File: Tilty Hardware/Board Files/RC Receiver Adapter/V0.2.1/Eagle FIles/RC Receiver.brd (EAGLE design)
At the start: 38.1 x 50.8 mm, 33 parts, among them U1 ATMEGA328P, U2 LM2931, U3 AP7313SOT23R, U4 PCA9306, Y1 16MHz

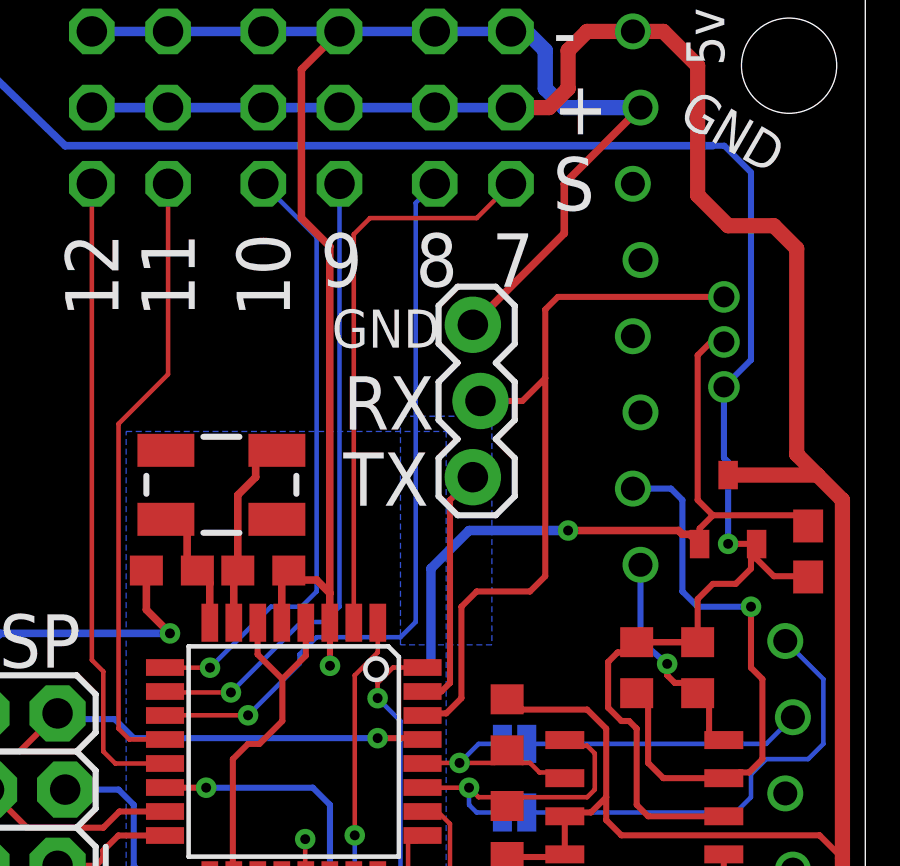
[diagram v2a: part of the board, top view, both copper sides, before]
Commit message: Moved serial breakout slightly
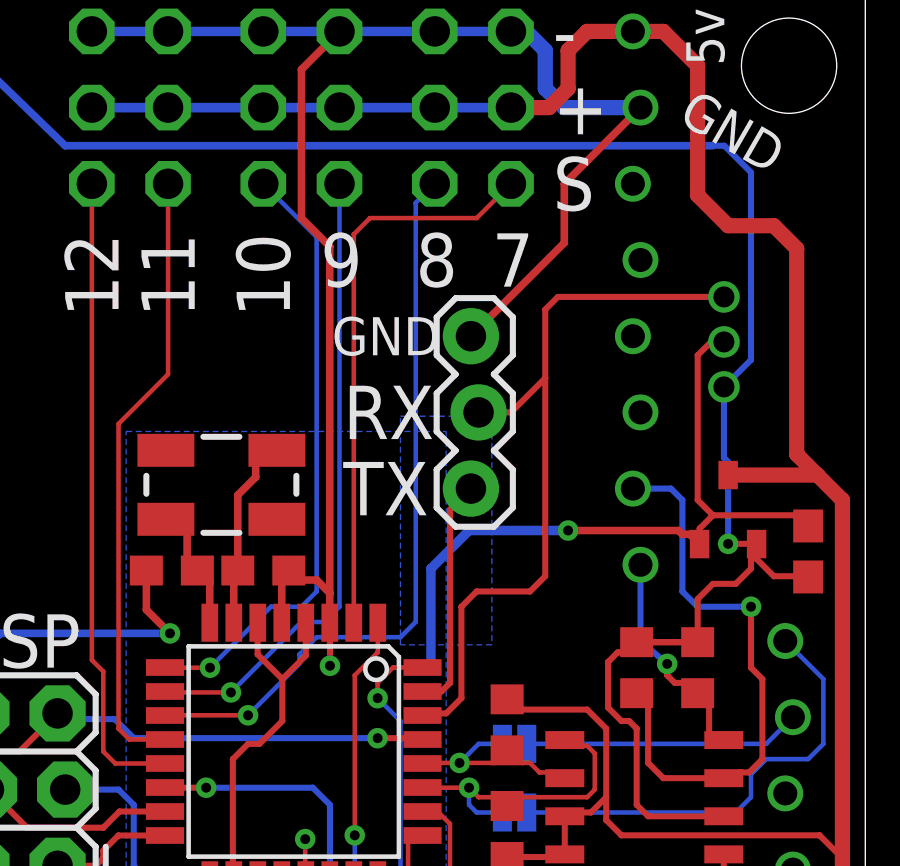
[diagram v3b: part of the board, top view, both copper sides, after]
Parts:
- moved JP9 0.39 mm to (25.1, 34.2)
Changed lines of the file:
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@@
 <text x="5.334" y="46.482" size="1.27" layer="25" ratio="15" rot="R75">3v3</text>
 <text x="35.306" y="9.906" size="1.27" layer="25" ratio="15" rot="R240">GND</text>
-<text x="20.701" y="36.1315" size="1.778" layer="25" ratio="12">RX</text>
-<text x="20.701" y="33.5915" size="1.778" layer="25" ratio="12">TX</text>
-<text x="20.32" y="38.862" size="1.27" layer="25" ratio="15">GND</text>
+<text x="20.701" y="35.814" size="1.778" layer="25" ratio="12">RX</text>
+<text x="20.701" y="33.274" size="1.778" layer="25" ratio="12">TX</text>
+<text x="20.32" y="38.608" size="1.27" layer="25" ratio="15">GND</text>
 </plain>
 <attributes>
@@
 <element name="SJ2" library="SparkFun-Passives" package="SJ_2S-NOTRACE" value="SOLDERJUMPERNC2" x="26.416" y="25.654" smashed="yes" rot="MR0"/>
 <element name="SJ3" library="SparkFun-Passives" package="SJ_2S-NOTRACE" value="SOLDERJUMPERNC2" x="26.416" y="23.368" smashed="yes" rot="MR0"/>
-<element name="JP9" library="SparkFun-Connectors" package="1X03_LOCK" value="" x="25.146" y="34.544" smashed="yes" rot="R90">
-<attribute name="VALUE" x="28.321" y="33.274" size="1.27" layer="27" rot="R90"/>
+<element name="JP9" library="SparkFun-Connectors" package="1X03_LOCK" value="" x="25.0825" y="34.163" smashed="yes" rot="R90">
+<attribute name="VALUE" x="28.2575" y="32.893" size="1.27" layer="27" rot="R90"/>
 </element>
 </elements>
@@
 <wire x1="7.62" y1="16.764" x2="7.62" y2="17.78" width="0.508" layer="1"/>
 <contactref element="JP9" pad="3"/>
-<wire x1="25.019" y1="39.624" x2="28.067" y2="42.672" width="0.254" layer="1"/>
-<wire x1="28.067" y1="42.672" x2="28.067" y2="44.323" width="0.254" layer="1"/>
+<wire x1="28.067" y1="42.3545" x2="28.067" y2="44.323" width="0.254" layer="1"/>
 <wire x1="28.067" y1="44.323" x2="30.607" y2="46.863" width="0.254" layer="1"/>
+<wire x1="24.9555" y1="39.243" x2="28.067" y2="42.3545" width="0.254" layer="1"/>
 </signal>
 <signal name="+24V">
@@
 <wire x1="33.3885" y1="40.5525" x2="27.8525" y2="40.5525" width="0.2032" layer="1"/>
 <wire x1="27.8525" y1="40.5525" x2="27.432" y2="40.132" width="0.2032" layer="1"/>
+<wire x1="27.432" y1="40.132" x2="27.432" y2="37.846" width="0.2032" layer="1"/>
 <wire x1="27.432" y1="37.846" x2="27.432" y2="31.242" width="0.2032" layer="1"/>
 <wire x1="27.432" y1="31.242" x2="26.924" y2="30.734" width="0.2032" layer="1"/>
@@
 <wire x1="23.4126" y1="26.67" x2="23.3426" y2="26.6" width="0.2032" layer="1"/>
 <contactref element="JP9" pad="2"/>
-<wire x1="27.432" y1="40.132" x2="27.432" y2="37.846" width="0.2032" layer="1"/>
-<wire x1="27.432" y1="37.846" x2="26.67" y2="37.084" width="0.2032" layer="1"/>
-<wire x1="26.67" y1="37.084" x2="25.273" y2="37.084" width="0.2032" layer="1"/>
+<wire x1="25.2095" y1="36.703" x2="26.289" y2="36.703" width="0.2032" layer="1"/>
+<wire x1="26.289" y1="36.703" x2="27.432" y2="37.846" width="0.2032" layer="1"/>
 </signal>
 <signal name="+3V3">
@@
 <wire x1="23.3426" y1="27.4" x2="23.971" y2="27.4" width="0.2032" layer="1"/>
 <wire x1="23.971" y1="27.4" x2="24.257" y2="27.686" width="0.2032" layer="1"/>
-<wire x1="24.257" y1="27.686" x2="24.257" y2="33.782" width="0.2032" layer="1"/>
-<wire x1="24.257" y1="33.782" x2="25.019" y2="34.544" width="0.2032" layer="1"/>
+<wire x1="24.257" y1="27.686" x2="24.257" y2="33.4645" width="0.2032" layer="1"/>
+<wire x1="24.257" y1="33.4645" x2="24.9555" y2="34.163" width="0.2032" layer="1"/>
 </signal>
 <signal name="STATUS_LED">
